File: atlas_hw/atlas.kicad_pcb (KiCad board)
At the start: 2 copper layers, 16 parts, among them J1 Micro_SD_Card_Det, J2 PSP_LCD, U1 STM32H743VITx, U10 NCP600SNADJ, U11 STM6601CA2BDM6F, U12 TPS63050, U2 nRF52810-QCxx, U3 W957D8MFYA, U4 LSF0108, U5 LSF0108, U6 LSF0108, U7 NCP600SNADJ, U8 TLV62569DBV, U9 TPS61070, Y1 32MHz, Y2 32.768kHz

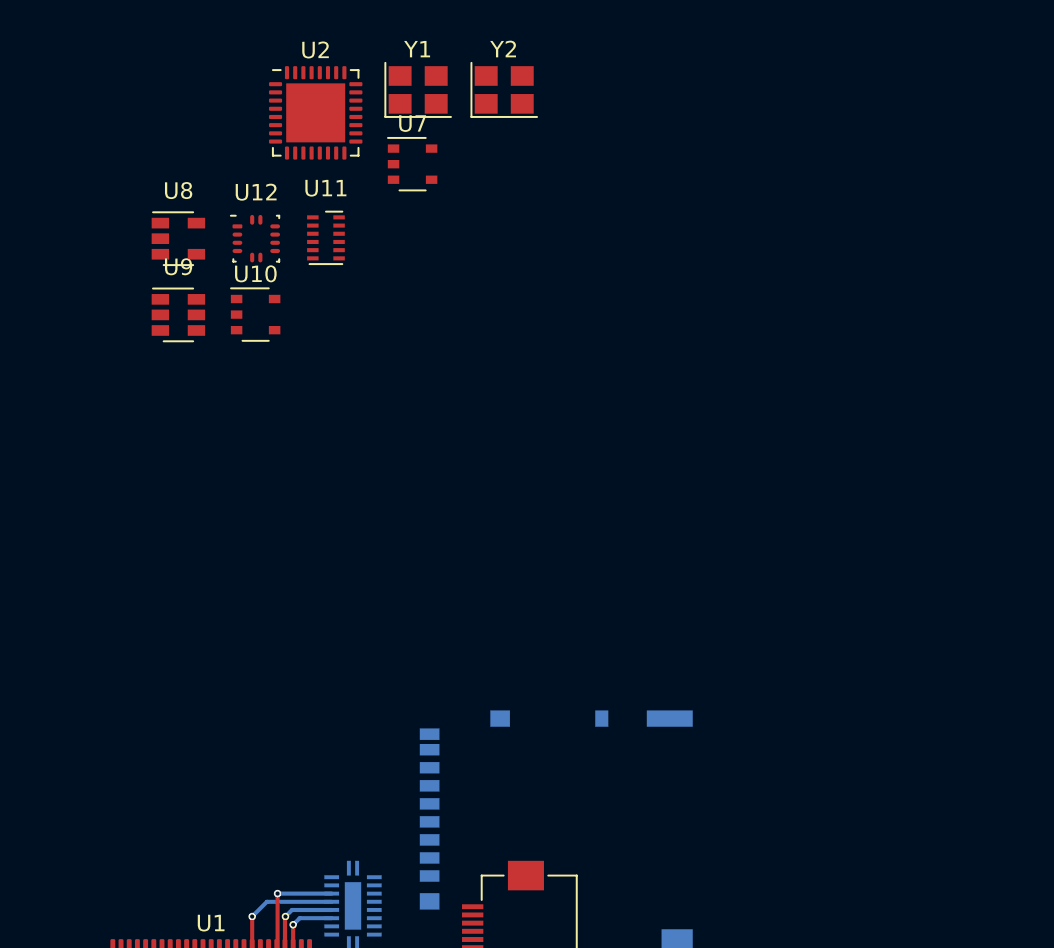
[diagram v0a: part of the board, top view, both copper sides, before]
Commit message: Added gps to sch and footprint work
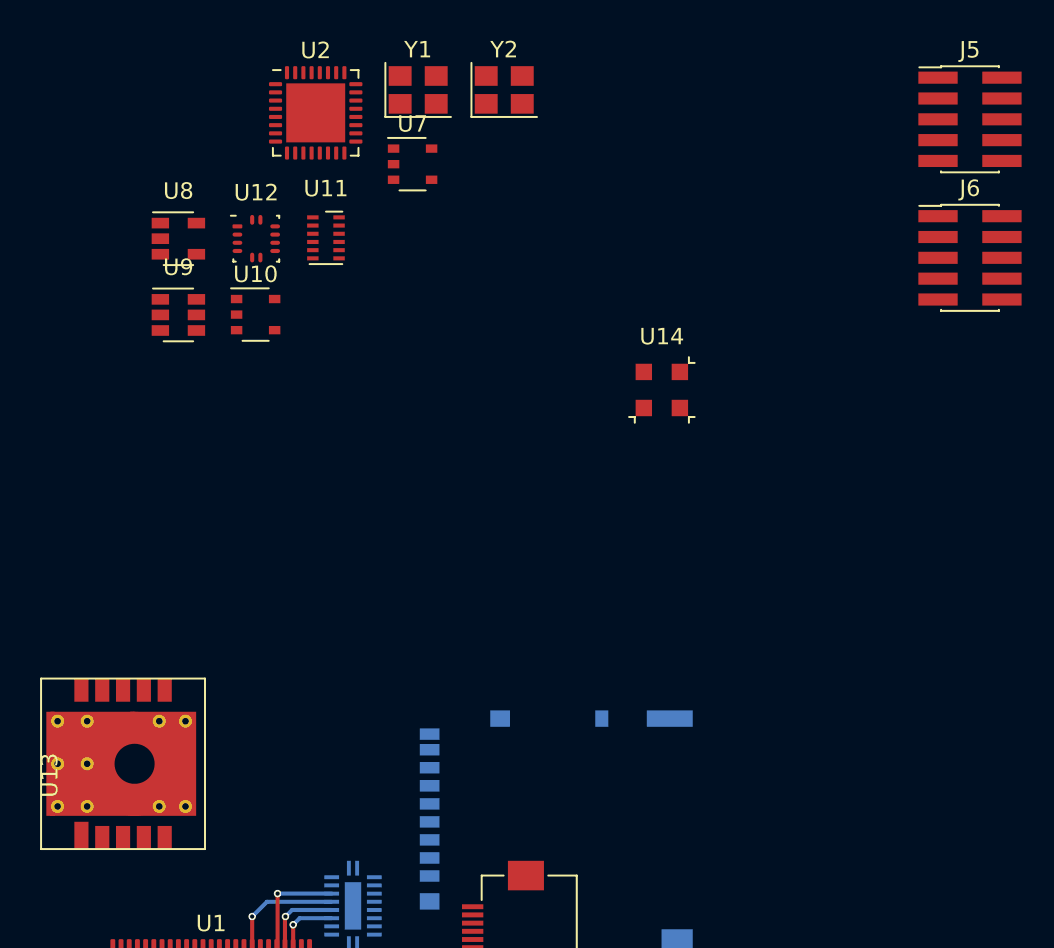
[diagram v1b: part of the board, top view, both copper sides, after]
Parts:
- added J5: DEBUG_STM, Connector_PinHeader_1.27mm:PinHeader_2x05_P1.27mm_Vertical_SMD, F.Cu at (154.7, 29.7)
- added J6: DEBUG_NRF, Connector_PinHeader_1.27mm:PinHeader_2x05_P1.27mm_Vertical_SMD, F.Cu at (154.7, 38.2)
- added U13: Wurth_2613011037000, atlas:Elara-1, F.Cu at (103.1, 68.8)
- added U14: MS5637, atlas:QFN-4_3x3_Pitch2mm, F.Cu at (135.9, 46.2)
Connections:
- U1 pad 89: Net-(U1-Pad89) -> /GPS_ON_OFF
- U1 pad 90: Net-(U1-Pad90) -> /GPS_WAKEUP
- U11 pad 4: /PWR_MCU_HOLD -> Net-(R18-Pad2)
- U2 pad 20: Net-(U2-Pad20) -> GND
- U2 pad 29: Net-(U2-Pad20) -> GND
- U2 pad 33: Net-(U2-Pad20) -> GND
- Y2 pad 1: /XL2_NRF -> /XL1_NRF
- Y2 pad 2: /XL1_NRF -> /XL2_NRF

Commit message: push to pcb
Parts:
- removed J5: DEBUG_STM, Connector_PinHeader_1.27mm:PinHeader_2x05_P1.27mm_Vertical_SMD
- removed J6: DEBUG_NRF, Connector_PinHeader_1.27mm:PinHeader_2x05_P1.27mm_Vertical_SMD
- removed Y1: 32MHz, Crystal:Crystal_SMD_3225-4Pin_3.2x2.5mm
- removed Y2: 32.768kHz, Crystal:Crystal_SMD_3225-4Pin_3.2x2.5mm
- added F1: B39162B8813P810, Filter:Filter_1109-5_1.1x0.9mm, F.Cu at (148.1, 98.8)
- added J10: PSP_LCD, Connector_FFC-FPC:Hirose_FH12-40S-0.5SH_1x40-1MP_P0.50mm_Horizontal, F.Cu at (136.5, 89.2)
- added J4: DEBUG_NRF, Connector_PinHeader_1.27mm:PinHeader_2x05_P1.27mm_Vertical_SMD, F.Cu at (159.4, 108.1)
- added J8: Micro_SD_Card_Det, Connector_Card:microSD_HC_Hirose_DM3D-SF, F.Cu at (157.5, 93.2)
- added Q1: Q_NMOS_DGS, Package_TO_SOT_SMD:SOT-23, F.Cu at (165.5, 118.2)
- added Q2: Q_NMOS_DGS, Package_TO_SOT_SMD:SOT-23, F.Cu at (181.2, 97.5)
- added Q3: Q_NMOS_DGS, Package_TO_SOT_SMD:SOT-23, F.Cu at (176.8, 105.2)
- added Q4: Q_NMOS_DGS, Package_TO_SOT_SMD:SOT-23, F.Cu at (171.0, 109.1)
- added Q5: Q_NMOS_DGS, Package_TO_SOT_SMD:SOT-23, F.Cu at (166.5, 113.7)
- added U15: TPS61073, Package_TO_SOT_SMD:SOT-23-6, F.Cu at (149.0, 117.8)
- added U16: PAM2841, Package_DFN_QFN:DFN-8-1EP_2x2mm_P0.5mm_EP0.9x1.5mm, F.Cu at (153.6, 118.7)
- added U17: NX3L1T3157, Package_TO_SOT_SMD:SOT-886, F.Cu at (148.1, 96.2)
- J1: value Micro_SD_Card_Det -> USB_C_Receptacle_USB2.0; footprint Connector_Card:microSD_HC_Hirose_DM3AT-SF-PEJM5 -> Connector_USB:USB_C_Receptacle_Amphenol_12401548E4-2A; moved to F.Cu
- J2: value PSP_LCD -> DEBUG_STM; footprint Connector_FFC-FPC:Hirose_FH12-40S-0.5SH_1x40-1MP_P0.50mm_Horizontal -> Connector_PinHeader_1.27mm:PinHeader_2x05_P1.27mm_Vertical_SMD
- U1: value STM32H743VITx -> STM32H723VITx
- U10: value NCP600SNADJ -> BQ25611D; footprint Package_SO:TSOP-5_1.65x3.05mm_P0.95mm -> Package_DFN_QFN:WQFN-24-1EP_4x4mm_P0.5mm_EP2.7x2.7mm_ThermalVias
- U12: value TPS63050 -> BGA725L6; footprint atlas:VQFN12_2.5x2.5_Pitch0.5mm -> atlas:TSLP-6-2
- U13: value Wurth_2613011037000 -> LSF0108; footprint atlas:Elara-1 -> Package_DFN_QFN:WQFN-20-1EP_2.5x4.5mm_P0.5mm_EP1x2.9mm
- U14: value MS5637 -> NPP600SNADJ; footprint atlas:QFN-4_3x3_Pitch2mm -> Package_SO:TSOP-5_1.65x3.05mm_P0.95mm
- U2: value nRF52810-QCxx -> W957A8MFYA5I; footprint Package_DFN_QFN:QFN-32-1EP_5x5mm_P0.5mm_EP3.6x3.6mm -> atlas:BGA-25_5x5_6.0x8.0mm
- U3: value W957D8MFYA -> MCP1811B; footprint atlas:BGA-25_5x5_6.0x8.0mm -> Package_TO_SOT_SMD:SOT-23; moved to F.Cu
- U4: value LSF0108 -> TLV62569DBV; footprint Package_DFN_QFN:WQFN-20-1EP_2.5x4.5mm_P0.5mm_EP1x2.9mm -> Package_TO_SOT_SMD:SOT-23-5; moved to F.Cu
- U5: value LSF0108 -> nRF52810-QCxx; footprint Package_DFN_QFN:WQFN-20-1EP_2.5x4.5mm_P0.5mm_EP1x2.9mm -> Package_DFN_QFN:QFN-32-1EP_5x5mm_P0.5mm_EP3.6x3.6mm; moved to F.Cu
- U6: value LSF0108 -> LC709203F; footprint Package_DFN_QFN:WQFN-20-1EP_2.5x4.5mm_P0.5mm_EP1x2.9mm -> atlas:WDFN-8_3x4mm_0.6mm_1.96x2.56mm; moved to F.Cu
- U7: value NCP600SNADJ -> Teseo-LIV3F; footprint Package_SO:TSOP-5_1.65x3.05mm_P0.95mm -> RF_Module:ublox_MAX
- U8: value TLV62569DBV -> MS5637; footprint Package_TO_SOT_SMD:SOT-23-5 -> atlas:QFN-4_3x3_Pitch2mm
- U9: value TPS61070 -> MC6470; footprint Package_TO_SOT_SMD:SOT-23-6 -> Package_LGA:LGA-12_2x2mm_P0.5mm
- moved U9 92.4 mm to (157.5, 118.7)
- moved U11 90.2 mm to (161.4, 114.6)
- moved U2 89.8 mm to (180.5, 90.5)
- moved U8 89.5 mm to (143.8, 118.3)
- moved U7 81.9 mm to (148.2, 109.7)
- moved U10 78.2 mm to (133.3, 116.7)
- moved U12 73.7 mm to (147.9, 100.9)
- moved U14 69.9 mm to (166.5, 109.1)
- moved U3 69.8 mm to (176.8, 100.6), turned to 0 degrees
- moved U13 50.5 mm to (144.3, 98.2)
- moved J2 46.0 mm to (169.7, 102.6), turned to 0 degrees
- moved J1 45.5 mm to (170.8, 92.1), turned to 0 degrees
- moved U6 44.3 mm to (138.8, 116.3)
- moved U4 39.5 mm to (157.0, 114.6)
- moved U5 33.2 mm to (126.5, 117.1)
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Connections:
- net /PWR_WKIP1_ONOFF renamed /STC911_INT
- net /SPI2_MISO_SENSOR renamed Net-(U1-Pad53)
- net /SPI2_MOSI_SENSOR renamed Net-(U1-Pad54)
- net /SPI2_SCK_SENSOR renamed Net-(U1-Pad52)
- net /USB_HS_D+ renamed /USB_STM_D+
- net /USB_HS_D- renamed /USB_STM_D-
- net Net-(R12-Pad1) renamed /CHG_STAT
- net Net-(U1-Pad16) renamed /BTN_ENTER
- J2 pad 1: GND -> /VCC_MCU_3V3
- J2 pad 10: /LCD_FFC_R5 -> /DEBUG_NRESET_STM
- J2 pad 2: GND -> /DEBUG_SWDIO_STM
- J2 pad 3: /VCC_LCD_IO -> GND
- J2 pad 4: /VCC_LCD_IO -> /DEBUG_SWDCLK_STM
- J2 pad 5: /LCD_FFC_R4 -> GND
- J2 pad 6: /LCD_FFC_R5 -> Net-(J2-Pad6)
- J2 pad 7: /LCD_FFC_R6 -> Net-(J2-Pad7)
- J2 pad 8: /LCD_FFC_R7 -> Net-(J2-Pad8)
- J2 pad 9: /LCD_FFC_R4 -> GND
- U1 pad 100: /VCC_MCU_LV -> /VCC_MCU_3V3
- U1 pad 11: /VCC_MCU_LV -> /VCC_MCU_3V3
- U1 pad 2: Net-(U1-Pad2) -> /NRF_INT
- U1 pad 23: Net-(U1-Pad23) -> /LC709203_INT
- U1 pad 27: /VCC_MCU_LV -> /VCC_MCU_3V3
- U1 pad 28: /LTDC_VSYNC -> /LTDC_VS
- U1 pad 3: Net-(U1-Pad3) -> /~USB_DET
- U1 pad 41: /OCTOSPIM_P1_NCS -> /OCTOSPIM_P1_NPS
- U1 pad 44: /LTDC_CLK -> /LTDC_CK
- U1 pad 50: /VCC_MCU_LV -> /VCC_MCU_3V3
- U1 pad 51: /OCTOSPIM_P1_NCLK -> /OCTOSPIM_P1_NPLK
- U1 pad 55: Net-(U1-Pad55) -> /MC6470_INTA
- U1 pad 56: Net-(U1-Pad56) -> /MC6470_INTM
- U1 pad 58: /LED_STATUS -> /STM_STATUS
- U1 pad 6: /VCC_CELL_OUT -> Net-(C6-Pad1)
- U1 pad 63: /LTDC_HSYNC -> /LTDC_HS
- U1 pad 7: /PWR_WKUP4_NRF -> /BQ25611_INT
- U1 pad 75: /VCC_MCU_LV -> /VCC_MCU_3V3
- U1 pad 87: /PWR_MCU_INT -> /PWR_BTN_OUT
- U1 pad 88: /PWR_BTN_OUT -> /PWR_MCU_INT
- U1 pad 89: /GPS_ON_OFF -> /GPS_RESET
- U1 pad 93: /I2C1_SDA_SYSTEM -> /I2C1_SCL_SYSTEM
- U10 pad 1: /VCC_LCD_PWR -> /USB_PORT_VBUS
- U10 pad 2: GND -> /USB_CHGR_D+
- U10 pad 3: /VCC_LCD_PWR -> /USB_CHGR_D-
- U10 pad 5: /VCC_LCD_IO -> /I2C1_SCL_SYSTEM
- U11 pad 1: /VCC_CELL_OUT -> /VCC_SYS
- U12 pad 1: Net-(L8-Pad1) (its old number) -> GND
- U12 pad 2: GND -> /GPS_VCC_RF
- U12 pad 4: /VDD_SD_3V3 -> GND
- U12 pad 6: GND -> /GPS_ANT_OFF
- U13 pad 1: /GPS_ON_OFF -> GND
- U13 pad 10: /LPUART1_TX_GPS -> /SDMMC1_D1
- U13 pad 2: Net-(Q2-Pad2) -> /VCC_MCU_3V3
- U13 pad 3: /LPUART1_RX_GPS -> Net-(R88-Pad1)
- U13 pad 4: /VCC_MCU_LV -> /SDMMC1_D2
- U13 pad 5: GND -> /SDMMC1_D3
- U13 pad 6: /GPS_WAKEUP -> /SDMMC1_CMD
- U13 pad 7: Net-(R22-Pad1) -> /SDMMC1_CKIN
- U13 pad 8: Net-(R17-Pad2) -> /SDMMC1_CK
- U13 pad 9: Net-(U13-Pad9) -> /SDMMC1_D0
- U14 pad 2: Net-(U14-Pad2) -> GND
- U4 pad 1: GND -> /EN_MCU_PWR
- U4 pad 2: /VCC_MCU_LV -> GND
- U4 pad 3: /LTDC_R4 -> Net-(L3-Pad1)
- U4 pad 4: /LTDC_R5 -> /VCC_SYS
- U4 pad 5: /LTDC_R6 -> Net-(R4-Pad1)
- U5 pad 1: GND -> /DEC1
- U5 pad 10: /LTDC_VSYNC -> /SP4_MOSI_NRF
- U5 pad 11: /LCD_FFC_VS -> /SP4_MISO_NRF
- U5 pad 12: /LCD_FFC_HS -> /SP4_SCK_NRF
- U5 pad 13: /LCD_FFC_DE -> /UART8_RX_NRF
- U5 pad 14: /LCD_FFC_CK -> /UART8_TX_NRF
- U5 pad 15: /LCD_FFC_B7 -> /NRF_STATUS
- U5 pad 16: /LCD_FFC_B6 -> /DEBUG_NRESET_NRF
- U5 pad 17: /LCD_FFC_B5 -> /DEBUG_SWDCLK_NRF
- U5 pad 18: /LCD_FFC_B4 -> /DEBUG_SWDIO_NRF
- U5 pad 19: /VCC_LCD_IO -> Net-(C14-Pad2)
- U5 pad 2: /VCC_MCU_LV -> /XL1_NRF
- U5 pad 20: /VCC_LCD_IO -> GND
- U5 pad 21: GND -> /DEC2
- U5 pad 3: /LTDC_B4 -> /XL2_NRF
- U5 pad 4: /LTDC_B5 -> Net-(U5-Pad4)
- U5 pad 5: /LTDC_B6 -> Net-(U5-Pad5)
- U5 pad 6: /LTDC_B7 -> Net-(U5-Pad6)
- U5 pad 7: /LTDC_CLK -> Net-(U5-Pad7)
- U5 pad 8: /LTDC_DE -> /NRF_INT
- U5 pad 9: /LTDC_HSYNC -> /VCC_MCU_3V3
- U6 pad 2: /VCC_MCU_LV -> GND
- U6 pad 3: GND -> /CELL_POS
- U6 pad 4: /SDMMC1_D2 -> /LC709203_INT
- U6 pad 5: /SDMMC1_D3 -> Net-(U6-Pad5)
- U6 pad 6: /SDMMC1_CMD -> Net-(U6-Pad6)
- U6 pad 7: /SDMMC1_CK -> (no net)
- U6 pad 8: /SDMMC1_D0 -> (no net)
- U6 pad 9: /SDMMC1_D1 -> (no net)
- U7 pad 1: /VDD_SD_3V3 -> GND
- U7 pad 2: GND -> /LPUART1_TX_GPS
- U7 pad 3: /VDD_SD_3V3 -> /LPUART1_RX_GPS
- U7 pad 4: Net-(R2-Pad1) (its old number) -> /GPS_1PPS
- U7 pad 5: /VDD_SD_IO_3V3_1V8 -> /GPS_WAKEUP
- U8 pad 1: /EN_MCU_PWR -> /VCC_MCU_3V3
- U8 pad 2: GND -> /I2C_SDA_SENSOR
- U8 pad 3: Net-(L7-Pad1) -> /I2C_SCL_SENSOR
- U8 pad 4: /VCC_CELL_OUT -> GND
- U9 pad 2: GND -> /I2C_SDA_SENSOR
- U9 pad 3: /EN_LCD_PWR -> /VCC_MCU_3V3
- U9 pad 5: /VCC_LCD_PWR -> /MC6470_INTA
- U9 pad 6: /VCC_CELL_OUT -> /MC6470_INTM
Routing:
- net /LTDC_R5: track 25.7 -> 0.00 mm, vias 1 -> 0
- net /LTDC_DE: track 25.1 -> 0.00 mm, vias 1 -> 0
- net /LTDC_B4: track 24.3 -> 0.00 mm, vias 1 -> 0
- net /LTDC_CLK: track 24.2 -> 0.00 mm, vias 1 -> 0
- net /LTDC_G7: track 23.3 -> 0.00 mm, vias 1 -> 0
- net /LTDC_R4: track 21.7 -> 0.00 mm, vias 1 -> 0
- net /LTDC_B7: track 21.3 -> 0.00 mm, vias 1 -> 0
- net /LTDC_R6: track 20.9 -> 0.00 mm, vias 1 -> 0
- net /LTDC_B5: track 20.2 -> 0.00 mm, vias 1 -> 0
- net /LTDC_R7: track 15.2 -> 0.00 mm, vias 1 -> 0
- net /LTDC_G4: track 15.0 -> 0.00 mm, vias 1 -> 0
- net /LTDC_G5: track 15.0 -> 0.00 mm, vias 1 -> 0
- net /LTDC_G6: track 14.7 -> 0.00 mm, vias 1 -> 0
- net /LTDC_B6: track 13.0 -> 0.00 mm, vias 1 -> 0
- net /OCTOSPIM_P1_IO4: track 10.7 -> 0.00 mm, vias 1 -> 0
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
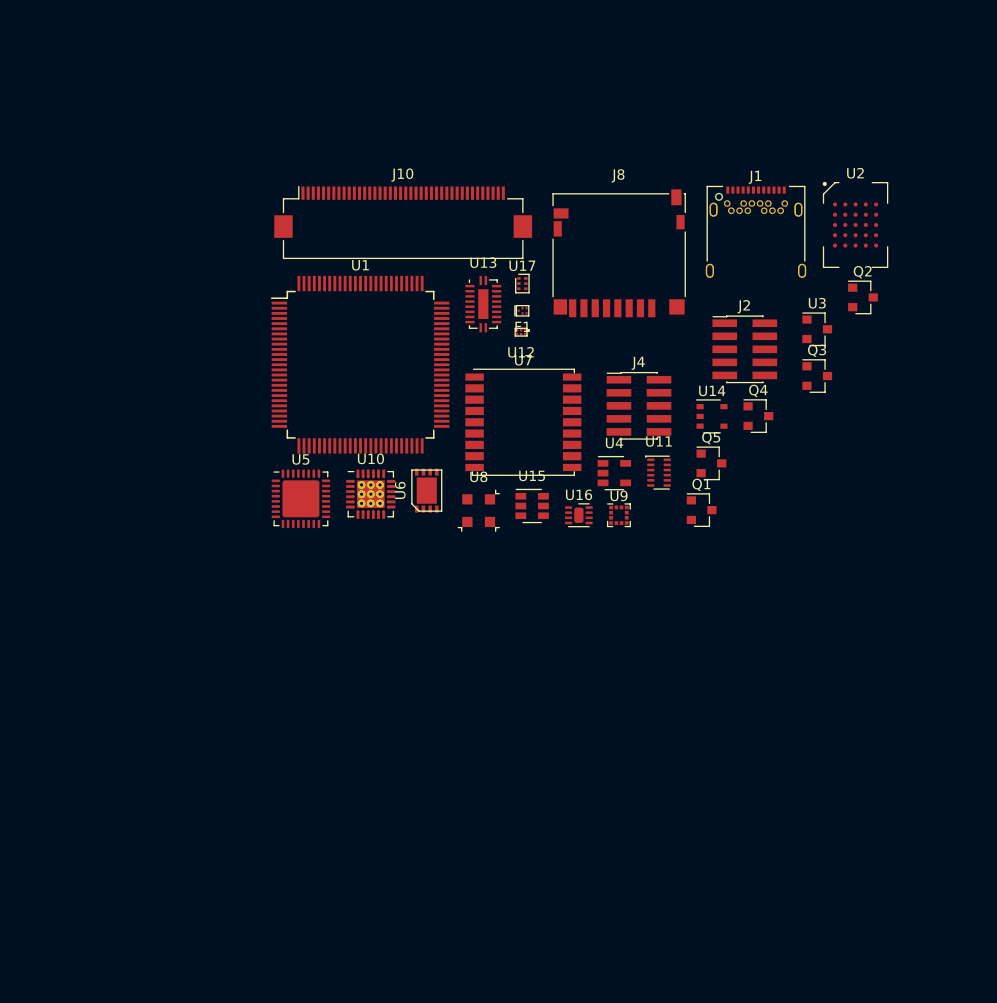
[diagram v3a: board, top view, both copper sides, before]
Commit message: Added additional passives, assigned fp
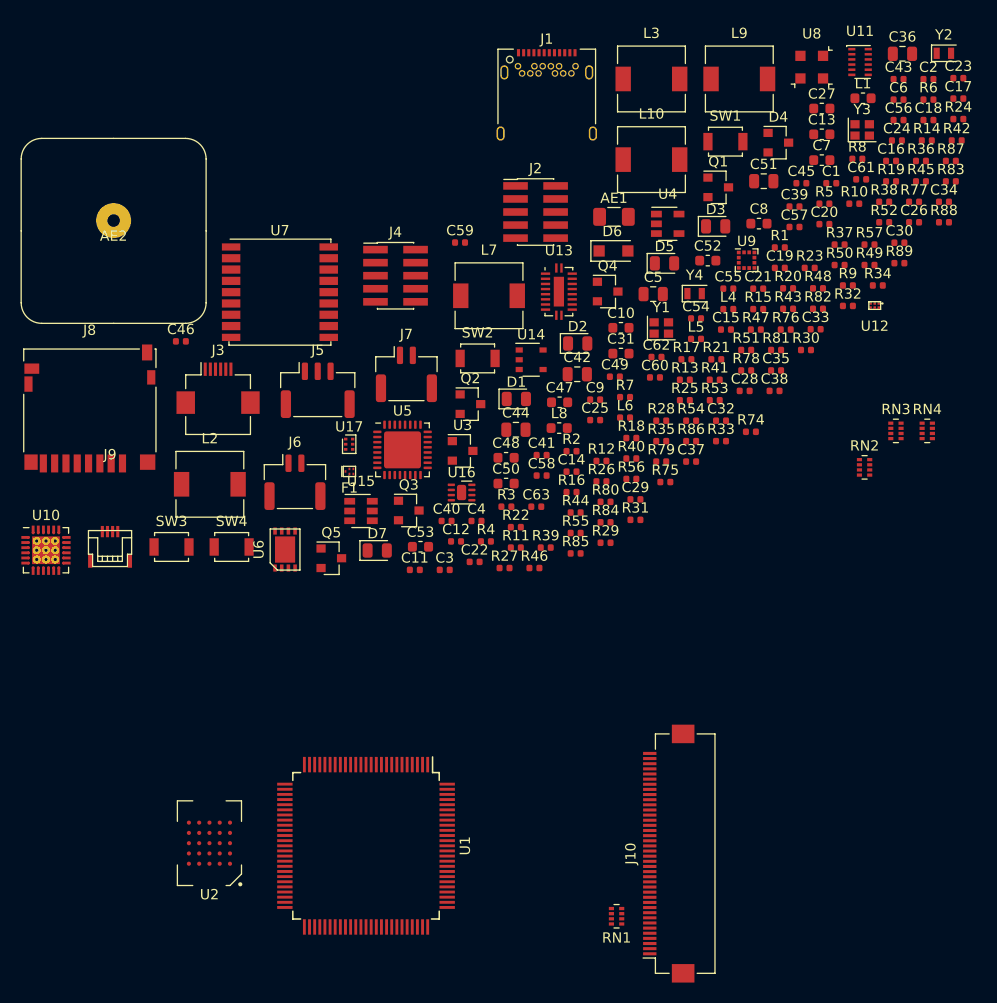
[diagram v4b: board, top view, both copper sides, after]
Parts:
- added AE1: CHIP, Inductor_SMD:L_1206_3216Metric, F.Cu at (157.0, 89.7)
- added AE2: 2088900001, atlas:2088900001, F.Cu at (108.3, 91.0)
- added C1: NP, Capacitor_SMD:C_0402_1005Metric, F.Cu at (178.1, 86.4)
- added C10: 1u, Capacitor_SMD:C_0603_1608Metric, F.Cu at (157.7, 100.5)
- added C11: 0.1u, Capacitor_SMD:C_0402_1005Metric, F.Cu at (137.6, 124.0)
- added C12: 100p, Capacitor_SMD:C_0402_1005Metric, F.Cu at (141.6, 121.3)
- added C13: 1u, Capacitor_SMD:C_0603_1608Metric, F.Cu at (177.2, 81.6)
- added C14: 1p, Capacitor_SMD:C_0402_1005Metric, F.Cu at (152.8, 114.5)
- added C15: NP, Capacitor_SMD:C_0402_1005Metric, F.Cu at (167.9, 100.6)
- added C16: 0.1u, Capacitor_SMD:C_0402_1005Metric, F.Cu at (183.9, 84.2)
- added C17: 1p, Capacitor_SMD:C_0402_1005Metric, F.Cu at (190.5, 78.2)
- added C18: 1p, Capacitor_SMD:C_0402_1005Metric, F.Cu at (187.6, 80.2)
- added C19: 22p, Capacitor_SMD:C_0402_1005Metric, F.Cu at (173.1, 94.6)
- added C2: 12p, Capacitor_SMD:C_0402_1005Metric, F.Cu at (187.6, 76.3)
- added C20: 2.2p, Capacitor_SMD:C_0402_1005Metric, F.Cu at (177.5, 90.4)
- added C21: 22p, Capacitor_SMD:C_0402_1005Metric, F.Cu at (171.0, 96.7)
- added C22: 0.1u, Capacitor_SMD:C_0402_1005Metric, F.Cu at (143.4, 123.2)
- added C23: 0.1u, Capacitor_SMD:C_0402_1005Metric, F.Cu at (190.5, 76.2)
- added C24: 0.1u, Capacitor_SMD:C_0402_1005Metric, F.Cu at (184.5, 82.2)
- added C25: 0.1u, Capacitor_SMD:C_0402_1005Metric, F.Cu at (155.1, 109.4)
- added C26: 0.1u, Capacitor_SMD:C_0402_1005Metric, F.Cu at (186.2, 90.2)
- added C27: 1u, Capacitor_SMD:C_0603_1608Metric, F.Cu at (177.2, 79.1)
- added C28: 0.1u, Capacitor_SMD:C_0402_1005Metric, F.Cu at (169.7, 106.6)
- added C29: 0.1u, Capacitor_SMD:C_0402_1005Metric, F.Cu at (159.1, 117.2)
- added C3: NP, Capacitor_SMD:C_0402_1005Metric, F.Cu at (140.5, 124.0)
- added C30: 0.1u, Capacitor_SMD:C_0402_1005Metric, F.Cu at (184.8, 92.2)
- added C31: 1u, Capacitor_SMD:C_0603_1608Metric, F.Cu at (157.7, 103.0)
- added C32: 0.1u, Capacitor_SMD:C_0402_1005Metric, F.Cu at (167.4, 109.5)
- added C33: 0.1u, Capacitor_SMD:C_0402_1005Metric, F.Cu at (176.6, 100.6)
- added C34: 0.1u, Capacitor_SMD:C_0402_1005Metric, F.Cu at (189.1, 88.2)
- added C35: 0.1u, Capacitor_SMD:C_0402_1005Metric, F.Cu at (172.8, 104.6)
- added C36: 10u, Capacitor_SMD:C_0805_2012Metric, F.Cu at (185.1, 73.8)
- added C37: 10u, Capacitor_SMD:C_0402_1005Metric, F.Cu at (164.5, 113.5)
- added C38: 0.1u, Capacitor_SMD:C_0402_1005Metric, F.Cu at (172.6, 106.6)
- added C39: 0.1u, Capacitor_SMD:C_0402_1005Metric, F.Cu at (174.5, 88.7)
- added C4: 12p, Capacitor_SMD:C_0402_1005Metric, F.Cu at (143.6, 119.3)
- added C40: 10u, Capacitor_SMD:C_0402_1005Metric, F.Cu at (140.7, 119.3)
- added C41: 47n, Capacitor_SMD:C_0402_1005Metric, F.Cu at (149.9, 112.9)
- added C42: 10u, Capacitor_SMD:C_0805_2012Metric, F.Cu at (153.4, 105.0)
- added C43: 120p, Capacitor_SMD:C_0402_1005Metric, F.Cu at (184.7, 76.3)
- added C44: 10u, Capacitor_SMD:C_0805_2012Metric, F.Cu at (147.4, 110.4)
- added C45: 0.1u, Capacitor_SMD:C_0402_1005Metric, F.Cu at (175.2, 86.4)
- added C46: 120p, Capacitor_SMD:C_0402_1005Metric, F.Cu at (114.8, 101.8)
- added C47: 1u, Capacitor_SMD:C_0603_1608Metric, F.Cu at (151.7, 107.7)
- added C48: 1u, Capacitor_SMD:C_0603_1608Metric, F.Cu at (146.5, 113.1)
- added C49: 0.1u, Capacitor_SMD:C_0402_1005Metric, F.Cu at (157.1, 105.2)
- added C5: 10u, Capacitor_SMD:C_0805_2012Metric, F.Cu at (160.8, 97.2)
- added C50: 1u, Capacitor_SMD:C_0603_1608Metric, F.Cu at (146.5, 115.6)
- added C51: 10u, Capacitor_SMD:C_0805_2012Metric, F.Cu at (171.6, 86.2)
- added C52: 1u, Capacitor_SMD:C_0603_1608Metric, F.Cu at (166.1, 93.9)
- added C53: 1u, Capacitor_SMD:C_0603_1608Metric, F.Cu at (138.1, 121.8)
- added C54: 0.1u, Capacitor_SMD:C_0402_1005Metric, F.Cu at (165.0, 99.6)
- added C55: 0.1u, Capacitor_SMD:C_0402_1005Metric, F.Cu at (168.1, 96.7)
- added C56: 0.1u, Capacitor_SMD:C_0402_1005Metric, F.Cu at (184.7, 80.2)
- added C57: 0.1u, Capacitor_SMD:C_0402_1005Metric, F.Cu at (174.5, 90.7)
- added C58: 0.1u, Capacitor_SMD:C_0402_1005Metric, F.Cu at (149.9, 114.8)
- added C59: 0.1u, Capacitor_SMD:C_0402_1005Metric, F.Cu at (142.0, 92.2)
- added C6: 0.1u, Capacitor_SMD:C_0402_1005Metric, F.Cu at (184.7, 78.3)
- added C60: 0.1u, Capacitor_SMD:C_0402_1005Metric, F.Cu at (161.0, 105.3)
- added C61: 0.1u, Capacitor_SMD:C_0402_1005Metric, F.Cu at (181.0, 86.0)
- added C62: 1u, Capacitor_SMD:C_0402_1005Metric, F.Cu at (161.1, 103.3)
- added C63: 1u, Capacitor_SMD:C_0402_1005Metric, F.Cu at (149.4, 117.9)
- added C7: 1u, Capacitor_SMD:C_0603_1608Metric, F.Cu at (177.2, 84.1)
- added C8: 1u, Capacitor_SMD:C_0603_1608Metric, F.Cu at (171.1, 90.3)
- added C9: 0.1u, Capacitor_SMD:C_0402_1005Metric, F.Cu at (155.1, 107.5)
- added D1: GPS_1PPS, LED_SMD:LED_0805_2012Metric, F.Cu at (147.5, 107.4)
- added D2: STM_STATUS, LED_SMD:LED_0805_2012Metric, F.Cu at (153.4, 102.0)
- added D3: NRF_STATUS, LED_SMD:LED_0805_2012Metric, F.Cu at (166.9, 90.6)
- added D4: DC, Package_TO_SOT_SMD:SOT-23, F.Cu at (173.0, 82.4)
- added D5: CHARGE_STATUS, LED_SMD:LED_0805_2012Metric, F.Cu at (161.9, 94.2)
- added D6: D_Schottky_Small_ALT, Diode_SMD:D_SOD-123F, F.Cu at (156.9, 93.0)
- added D7: USB_DETECT, LED_SMD:LED_0805_2012Metric, F.Cu at (133.9, 122.1)
- added J3: PSP_TOUCH, Connector_FFC-FPC:Hirose_FH12-6S-0.5SH_1x06-1MP_P0.50mm_Horizontal, F.Cu at (118.4, 106.3)
- added J5: CELL_THERM, Connector_JST:JST_GH_SM03B-GHS-TB_1x03-1MP_P1.25mm_Horizontal, F.Cu at (128.1, 106.5)
- added J6: CELL_BARE, Connector_JST:JST_GH_SM02B-GHS-TB_1x02-1MP_P1.25mm_Horizontal, F.Cu at (125.9, 115.5)
- added J7: AUX_THERM, Connector_JST:JST_GH_SM02B-GHS-TB_1x02-1MP_P1.25mm_Horizontal, F.Cu at (136.8, 105.0)
- added J9: PSP_LCD_BL, atlas:Kyocera_046298_004_1x04_P0.5mm_Bottom, F.Cu at (107.9, 120.3)
- added L1: 3.9n, Inductor_SMD:L_0603_1608Metric, F.Cu at (181.2, 78.1)
- added L10: 3.9n, Inductor_SMD:L_6.3x6.3_H3, F.Cu at (160.6, 84.1)
- added L2: 15u, Inductor_SMD:L_6.3x6.3_H3, F.Cu at (117.6, 115.7)
- added L3: L_Small, Inductor_SMD:L_6.3x6.3_H3, F.Cu at (160.6, 76.2)
- added L4: 3.9n, Inductor_SMD:L_0402_1005Metric, F.Cu at (168.1, 98.6)
- added L5: NP, Inductor_SMD:L_0402_1005Metric, F.Cu at (165.0, 101.5)
- added L6: 3.9n, Inductor_SMD:L_0402_1005Metric, F.Cu at (158.1, 109.2)
- added L7: 1u, Inductor_SMD:L_6.3x6.3_H3, F.Cu at (144.8, 97.3)
- added L8: 5n6, Inductor_SMD:L_0603_1608Metric, F.Cu at (151.6, 110.2)
- added L9: L_Small, Inductor_SMD:L_6.3x6.3_H3, F.Cu at (169.2, 76.2)
- added R1: 0, Resistor_SMD:R_0402_1005Metric, F.Cu at (173.1, 92.6)
- added R10: 1k, Resistor_SMD:R_0402_1005Metric, F.Cu at (180.4, 88.4)
- added R11: 1k, Resistor_SMD:R_0402_1005Metric, F.Cu at (147.4, 121.9)
- added R12: 5.1k, Resistor_SMD:R_0402_1005Metric, F.Cu at (155.8, 113.4)
- added R13: 5.1k, Resistor_SMD:R_0402_1005Metric, F.Cu at (163.9, 105.5)
- added R14: 0, Resistor_SMD:R_0402_1005Metric, F.Cu at (187.4, 82.2)
- added R15: 0, Resistor_SMD:R_0402_1005Metric, F.Cu at (171.0, 98.6)
- added R16: 0, Resistor_SMD:R_0402_1005Metric, F.Cu at (152.8, 116.5)
- added R17: 0, Resistor_SMD:R_0402_1005Metric, F.Cu at (164.0, 103.5)
- added R18: NP, Resistor_SMD:R_0402_1005Metric, F.Cu at (158.7, 111.2)
- added R19: 0, Resistor_SMD:R_0402_1005Metric, F.Cu at (183.9, 86.2)
- added R2: 0, Resistor_SMD:R_0402_1005Metric, F.Cu at (152.8, 112.5)
- added R20: NP, Resistor_SMD:R_0402_1005Metric, F.Cu at (173.9, 96.6)
- added R21: NP, Resistor_SMD:R_0402_1005Metric, F.Cu at (166.9, 103.5)
- added R22: NP, Resistor_SMD:R_0402_1005Metric, F.Cu at (147.4, 119.9)
- added R23: 100k, Resistor_SMD:R_0402_1005Metric, F.Cu at (176.0, 94.6)
- added R24: 0, Resistor_SMD:R_0402_1005Metric, F.Cu at (190.5, 80.1)
- added R25: 10k, Resistor_SMD:R_0402_1005Metric, F.Cu at (163.9, 107.5)
- added R26: NP, Resistor_SMD:R_0402_1005Metric, F.Cu at (155.8, 115.4)
- added R27: NP, Resistor_SMD:R_0402_1005Metric, F.Cu at (146.3, 123.8)
- added R28: NP, Resistor_SMD:R_0402_1005Metric, F.Cu at (161.6, 109.5)
- added R29: NP, Resistor_SMD:R_0402_1005Metric, F.Cu at (156.2, 121.4)
- added R3: 0, Resistor_SMD:R_0402_1005Metric, F.Cu at (146.5, 117.9)
- added R30: 10k, Resistor_SMD:R_0402_1005Metric, F.Cu at (175.7, 102.6)
- added R31: 100k, Resistor_SMD:R_0402_1005Metric, F.Cu at (159.1, 119.2)
- added R32: 100k, Resistor_SMD:R_0402_1005Metric, F.Cu at (179.7, 98.3)
- added R33: 100k, Resistor_SMD:R_0402_1005Metric, F.Cu at (167.4, 111.5)
- added R34: 100k, Resistor_SMD:R_0402_1005Metric, F.Cu at (182.7, 96.3)
- added R35: 1k, Resistor_SMD:R_0402_1005Metric, F.Cu at (161.6, 111.5)
- added R36: 100k, Resistor_SMD:R_0402_1005Metric, F.Cu at (186.9, 84.2)
- added R37: 1k, Resistor_SMD:R_0402_1005Metric, F.Cu at (178.9, 92.4)
- added R38: 100k, Resistor_SMD:R_0402_1005Metric, F.Cu at (183.3, 88.2)
- added R39: 100k, Resistor_SMD:R_0402_1005Metric, F.Cu at (150.3, 121.9)
- added R4: 200k, Resistor_SMD:R_0402_1005Metric, F.Cu at (144.5, 121.3)
- added R40: 0, Resistor_SMD:R_0402_1005Metric, F.Cu at (158.7, 113.2)
- added R41: NP, Resistor_SMD:R_0402_1005Metric, F.Cu at (166.8, 105.5)
- added R42: NP, Resistor_SMD:R_0402_1005Metric, F.Cu at (190.3, 82.2)
- added R43: 0, Resistor_SMD:R_0402_1005Metric, F.Cu at (173.9, 98.6)
- added R44: 0, Resistor_SMD:R_0402_1005Metric, F.Cu at (153.2, 118.4)
- added R45: NP, Resistor_SMD:R_0402_1005Metric, F.Cu at (186.9, 86.2)
- added R46: 0, Resistor_SMD:R_0402_1005Metric, F.Cu at (149.2, 123.8)
- added R47: 100k, Resistor_SMD:R_0402_1005Metric, F.Cu at (170.8, 100.6)
- added R48: NP, Resistor_SMD:R_0402_1005Metric, F.Cu at (176.8, 96.6)
- added R49: NP, Resistor_SMD:R_0402_1005Metric, F.Cu at (181.8, 94.4)
- added R5: 100k, Resistor_SMD:R_0402_1005Metric, F.Cu at (177.5, 88.4)
- added R50: NP, Resistor_SMD:R_0402_1005Metric, F.Cu at (178.9, 94.4)
- added R51: NP, Resistor_SMD:R_0402_1005Metric, F.Cu at (169.8, 102.6)
- added R52: NP, Resistor_SMD:R_0402_1005Metric, F.Cu at (183.3, 90.2)
- added R53: NP, Resistor_SMD:R_0402_1005Metric, F.Cu at (166.8, 107.5)
- added R54: 10k, Resistor_SMD:R_0402_1005Metric, F.Cu at (164.5, 109.5)
- added R55: 100k, Resistor_SMD:R_0402_1005Metric, F.Cu at (153.2, 120.4)
- added R56: NP, Resistor_SMD:R_0402_1005Metric, F.Cu at (158.7, 115.2)
- added R57: NP, Resistor_SMD:R_0402_1005Metric, F.Cu at (181.8, 92.4)
- added R6: 100k, Resistor_SMD:R_0402_1005Metric, F.Cu at (187.6, 78.3)
- added R7: 100k, Resistor_SMD:R_0402_1005Metric, F.Cu at (158.1, 107.2)
- added R74: NP, Resistor_SMD:R_0402_1005Metric, F.Cu at (170.3, 110.6)
- added R75: 200k, Resistor_SMD:R_0402_1005Metric, F.Cu at (162.0, 115.5)
- added R76: 250k, Resistor_SMD:R_0402_1005Metric, F.Cu at (173.7, 100.6)
- added R77: NP, Resistor_SMD:R_0402_1005Metric, F.Cu at (186.2, 88.2)
- added R78: 4.7k, Resistor_SMD:R_0402_1005Metric, F.Cu at (169.8, 104.6)
- added R79: 4.7k, Resistor_SMD:R_0402_1005Metric, F.Cu at (161.6, 113.5)
- added R8: 100k, Resistor_SMD:R_0402_1005Metric, F.Cu at (180.7, 84.0)
- added R80: 0, Resistor_SMD:R_0402_1005Metric, F.Cu at (156.2, 117.4)
- added R81: 0, Resistor_SMD:R_0402_1005Metric, F.Cu at (172.8, 102.6)
- added R82: NP, Resistor_SMD:R_0402_1005Metric, F.Cu at (176.8, 98.6)
- added R83: 0, Resistor_SMD:R_0402_1005Metric, F.Cu at (189.8, 86.2)
- added R84: 0, Resistor_SMD:R_0402_1005Metric, F.Cu at (156.2, 119.4)
- added R85: 100k, Resistor_SMD:R_0402_1005Metric, F.Cu at (153.2, 122.4)
- added R86: 100k, Resistor_SMD:R_0402_1005Metric, F.Cu at (164.5, 111.5)
- added R87: 1k, Resistor_SMD:R_0402_1005Metric, F.Cu at (189.8, 84.2)
- added R88: 0, Resistor_SMD:R_0402_1005Metric, F.Cu at (189.1, 90.2)
- added R89: 0, Resistor_SMD:R_0402_1005Metric, F.Cu at (184.8, 94.2)
- added R9: 1k, Resistor_SMD:R_0402_1005Metric, F.Cu at (179.7, 96.3)
- added RN1: R_Pack04, Resistor_SMD:R_Array_Concave_4x0402, F.Cu at (157.2, 157.7)
- added RN2: R_Pack04, Resistor_SMD:R_Array_Concave_4x0402, F.Cu at (181.4, 114.0)
- added RN3: R_Pack04, Resistor_SMD:R_Array_Concave_4x0402, F.Cu at (184.4, 110.5)
- added RN4: R_Pack04, Resistor_SMD:R_Array_Concave_4x0402, F.Cu at (187.5, 110.5)
- added SW1: SReset, Button_Switch_SMD:SW_SPST_B3U-1000P, F.Cu at (167.8, 82.3)
- added SW2: Power, Button_Switch_SMD:SW_SPST_B3U-1000P, F.Cu at (143.7, 103.4)
- added SW3: ResetSTM, Button_Switch_SMD:SW_SPST_B3U-1000P, F.Cu at (113.9, 121.8)
- added SW4: ResetNRF, Button_Switch_SMD:SW_SPST_B3U-1000P, F.Cu at (119.8, 121.8)
- added Y1: 16M, Crystal:Crystal_SMD_2016-4Pin_2.0x1.6mm, F.Cu at (161.6, 100.5)
- added Y2: 32k, Crystal:Crystal_SMD_2012-2Pin_2.0x1.2mm, F.Cu at (189.1, 73.7)
- added Y3: 32M, Crystal:Crystal_SMD_2016-4Pin_2.0x1.6mm, F.Cu at (181.1, 81.2)
- added Y4: 32k, Crystal:Crystal_SMD_2012-2Pin_2.0x1.2mm, F.Cu at (164.8, 97.1)
- moved U2 87.0 mm to (117.6, 150.6), turned to 180 degrees
- moved J10 67.6 mm to (162.3, 151.6), turned to 90 degrees
- moved U8 54.0 mm to (176.2, 75.1)
- moved J8 53.7 mm to (106.0, 108.3)
- moved U1 46.8 mm to (132.8, 150.9), turned to 270 degrees
- moved U11 44.5 mm to (180.9, 74.6)
- moved Q3 41.9 mm to (137.0, 118.2)
- moved Q2 39.6 mm to (143.0, 107.9)
- moved Q5 38.1 mm to (129.5, 122.9)
- moved U3 36.5 mm to (142.2, 112.4)
- moved U12 34.5 mm to (182.4, 98.3)
- moved U10 32.1 mm to (101.7, 122.1)
- moved Q1 31.5 mm to (167.1, 86.8)
- moved U9 27.8 mm to (169.9, 93.9)
- moved J4 26.9 mm to (135.7, 95.4)
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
